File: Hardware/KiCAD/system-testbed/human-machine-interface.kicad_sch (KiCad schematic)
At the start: 2 parts, among them SW21 RotaryEncoder_Switch

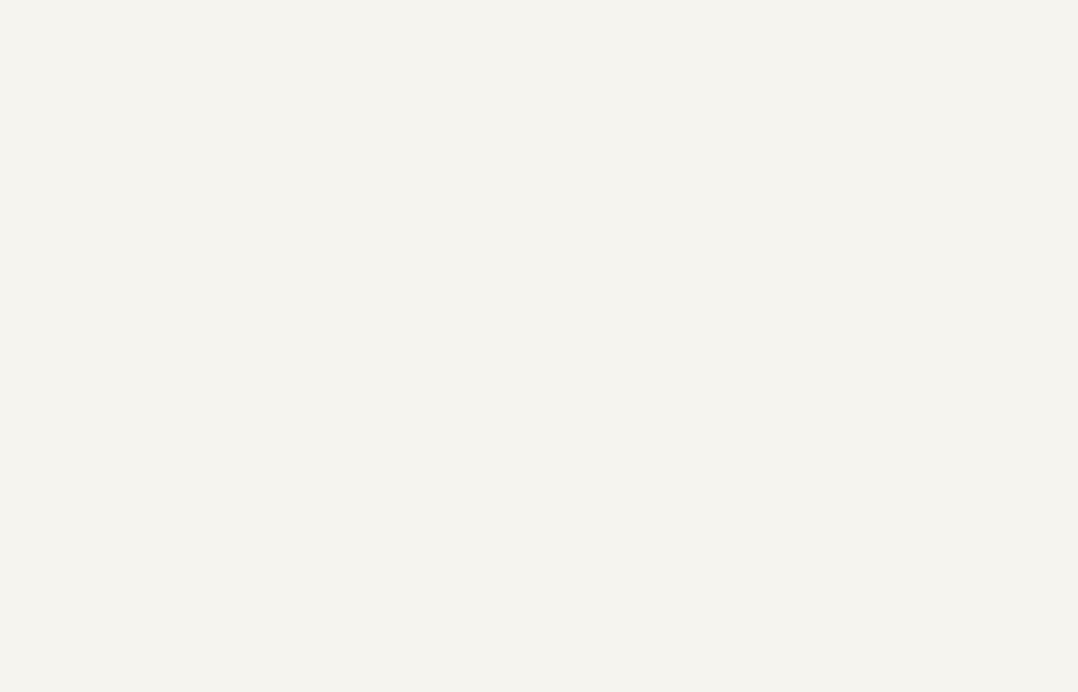
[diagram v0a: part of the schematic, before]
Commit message: feat: capture EYESPI display connectors #15
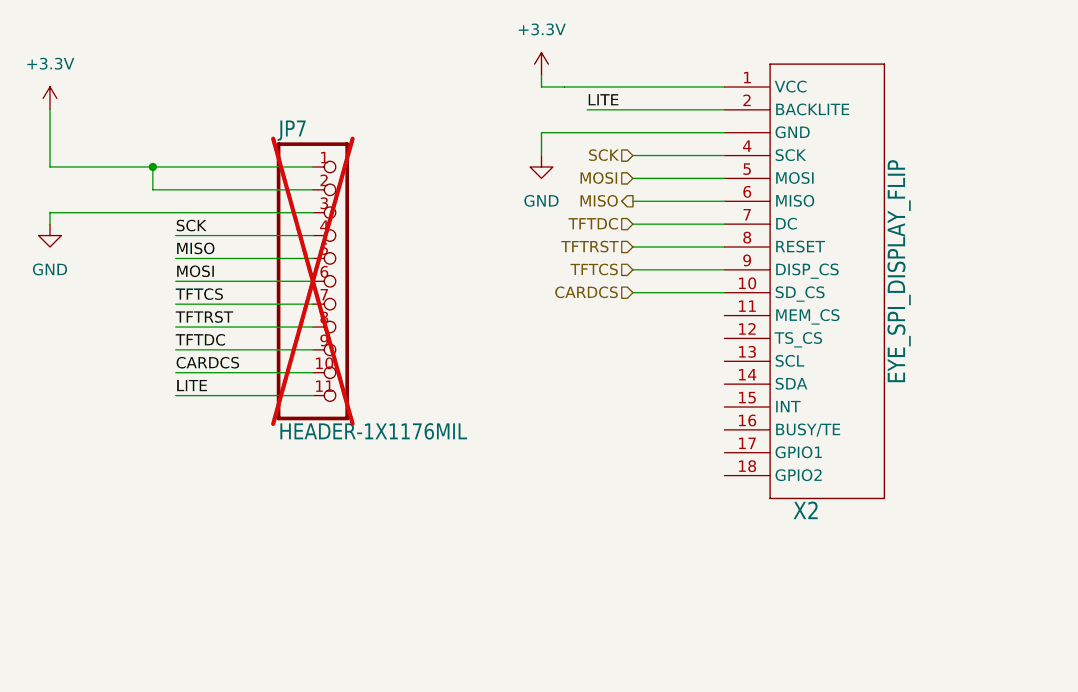
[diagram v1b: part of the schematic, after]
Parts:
- added JP7: HEADER-1X1176MIL, Display:1X11_ROUND_76, symbol Display-eagle-import:HEADER-1X1176MIL
- added X2: EYE_SPI_DISPLAY_FLIP, Display:EYE_SPI_DISPLAY_BOTCONTACT, symbol Display-eagle-import:EYE_SPI_DISPLAY_FLIP
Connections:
- net +3.3V: now also JP7.1, JP7.2, X2.1 (VCC)
- net GND: now also JP7.3, X2.3 (GND), X2.SUPPORT1 (GND), X2.SUPPORT2 (GND)
- new net CARDCS: JP7.10, X2.10 (SD_CS)
- new net LITE: JP7.11, X2.2 (BACKLITE)
- new net MISO: JP7.5, X2.6 (MISO)
- new net MOSI: JP7.6, X2.5 (MOSI)
- new net SCK: JP7.4, X2.4 (SCK)
- new net TFTCS: JP7.7, X2.9 (DISP_CS)
- new net TFTDC: JP7.9, X2.7 (DC)
- new net TFTRST: JP7.8, X2.8 (RESET)

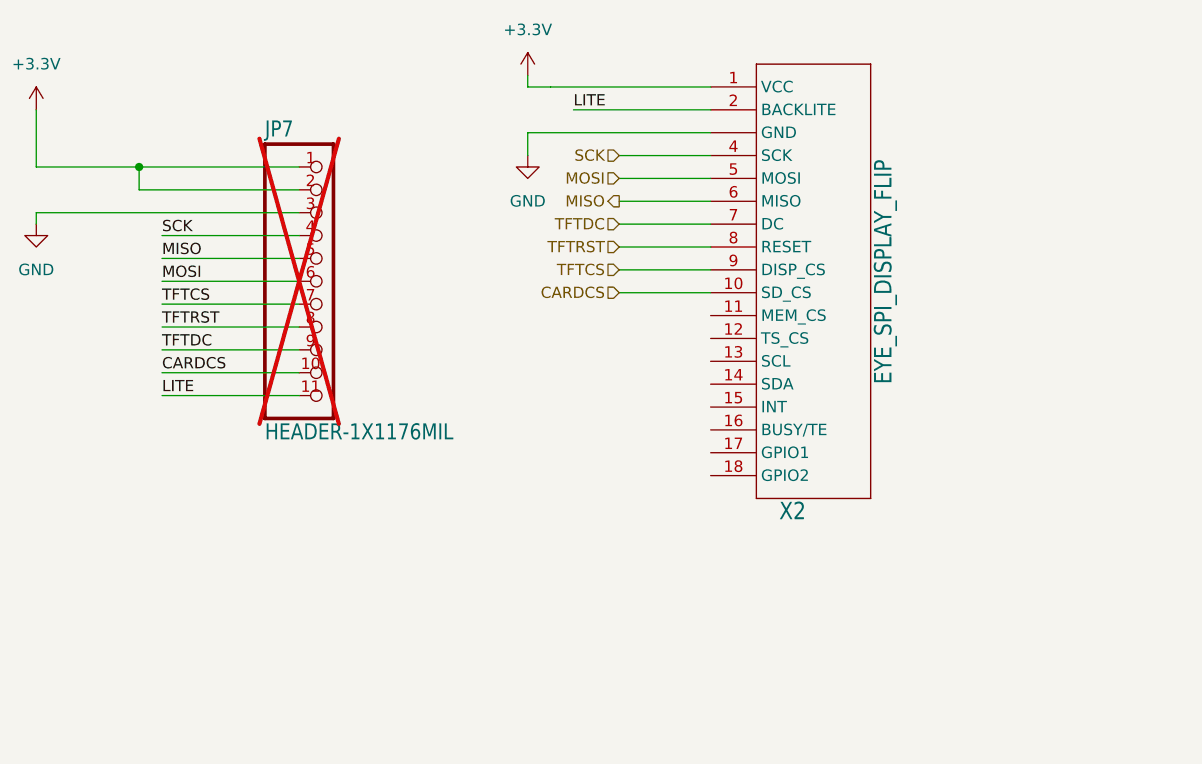
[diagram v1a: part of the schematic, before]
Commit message: fix: create real EYESPI FPC connector symbol and footprint #57
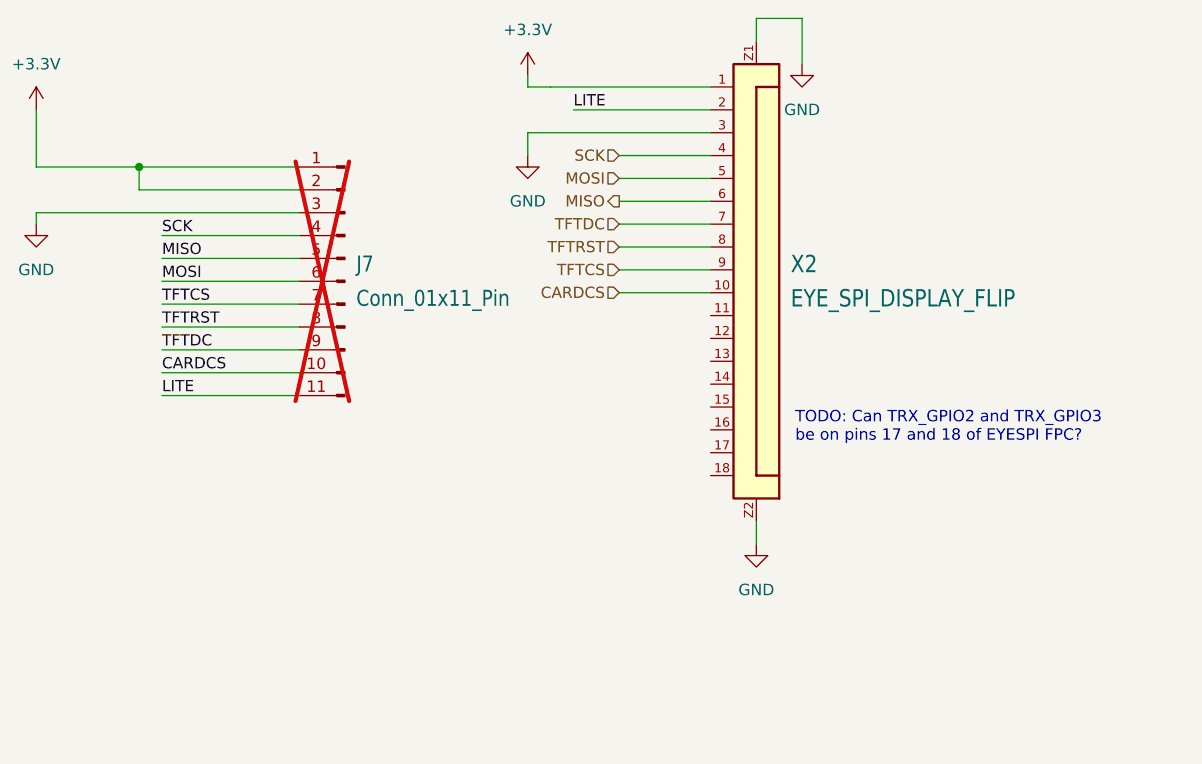
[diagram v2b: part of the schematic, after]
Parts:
- J7: renamed from JP7; value HEADER-1X1176MIL -> Conn_01x11_Pin; symbol Display-eagle-import:HEADER-1X1176MIL -> Connector:Conn_01x11_Pin
- X2: footprint Display:EYE_SPI_DISPLAY_BOTCONTACT -> capstone-project:Adafruit EYESPI FPC Connector; symbol Display-eagle-import:EYE_SPI_DISPLAY_FLIP -> capstone-project:Adafruit EYESPI FPC Connector
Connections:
- net GND: now also X2.Z1, X2.Z2; no longer X2.SUPPORT1 (GND), X2.SUPPORT2 (GND)
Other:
- note added: "TODO: Can TRX_GPIO2 and TRX_GPIO3 be on pins 17 and 18 of EYESPI FPC?"

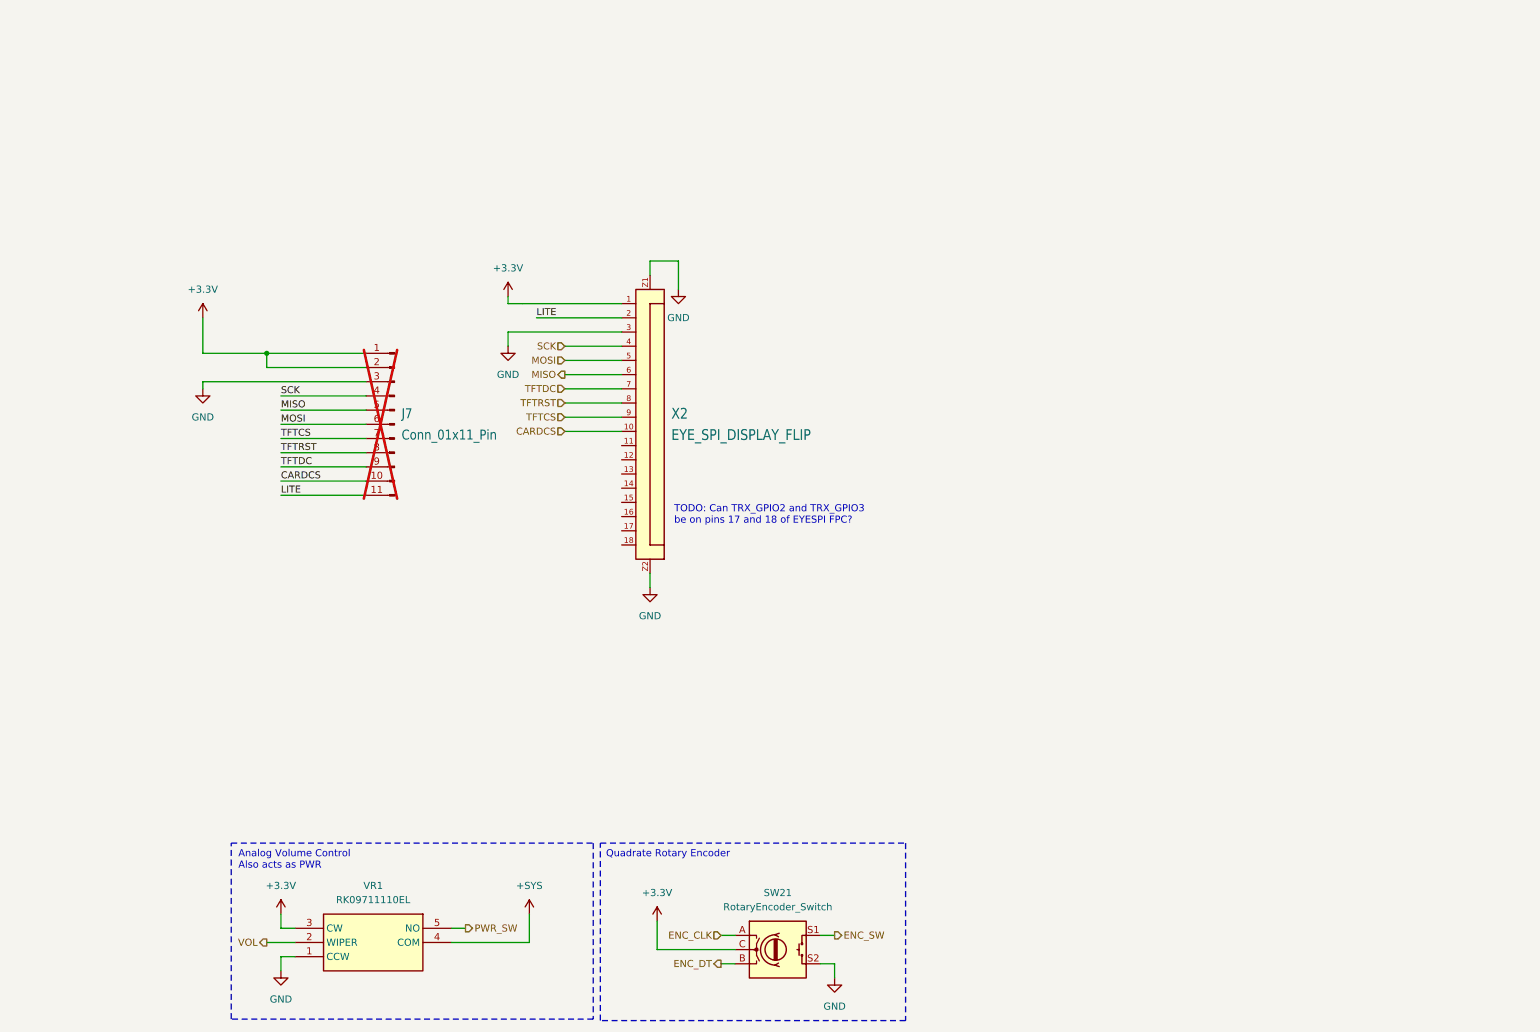
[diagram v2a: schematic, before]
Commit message: fix: move port expander over to HMI schematic #15 #33
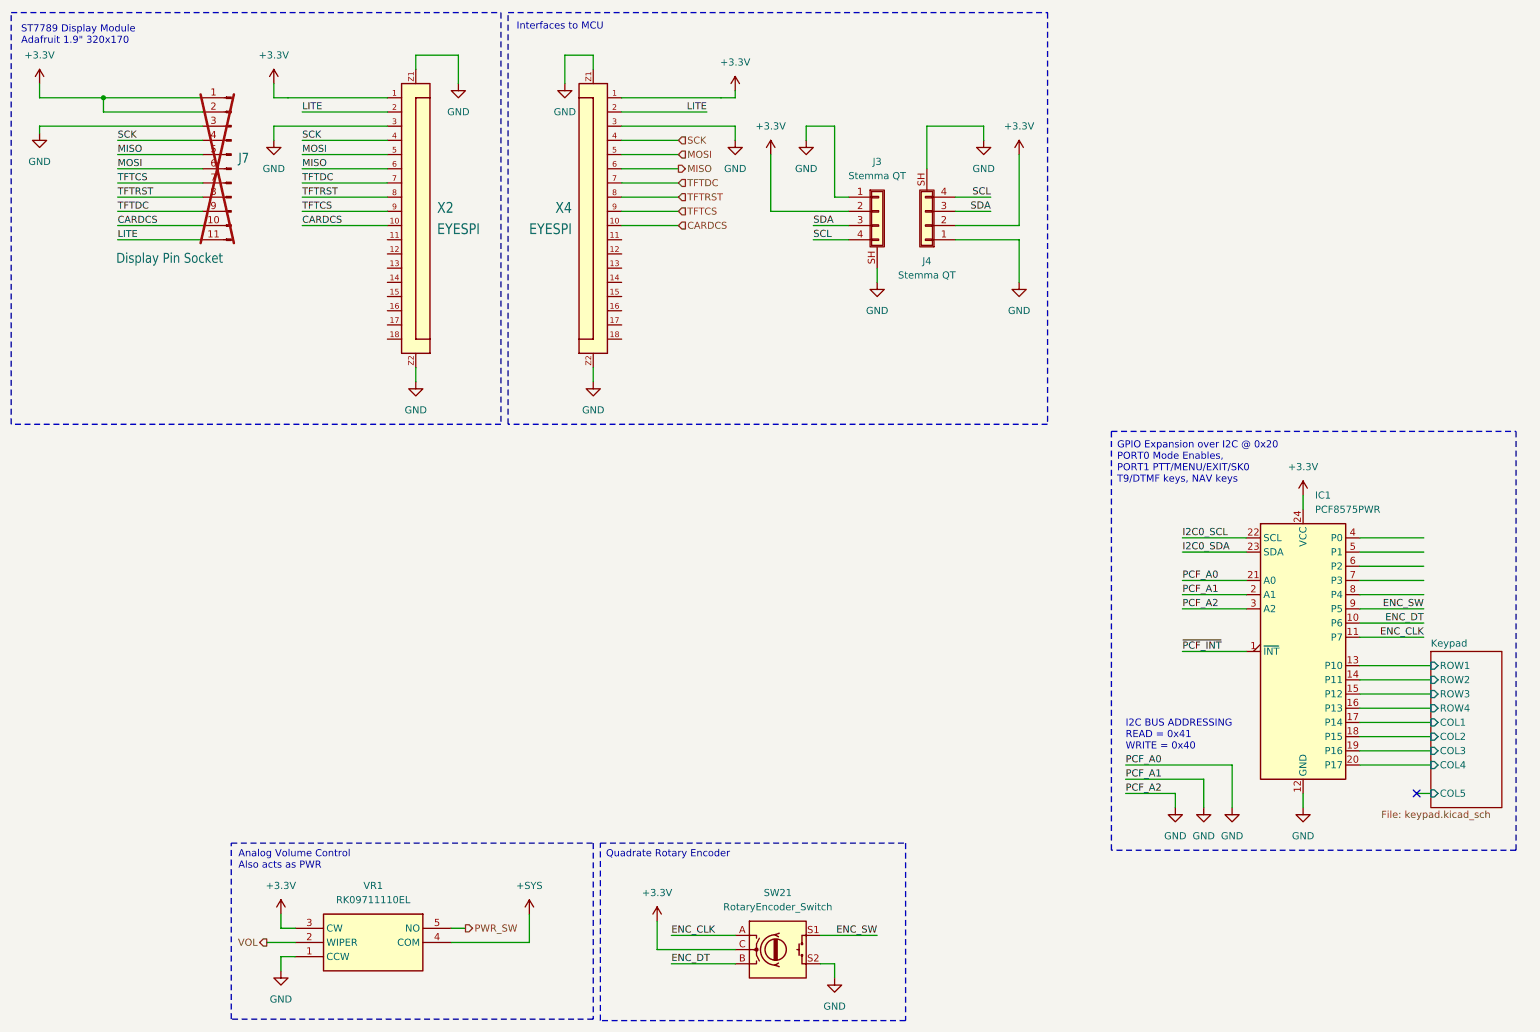
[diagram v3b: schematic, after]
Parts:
- added IC1: PCF8575PWR, Package_SO:SSOP-24_5.3x8.2mm_P0.65mm, symbol Interface_Expansion:PCF8575DBR
- added J3, J4: Stemma QT, Connector_JST:JST_SH_SM04B-SRSS-TB_1x04-1MP_P1.00mm_Horizontal, symbol Connector_Generic_Shielded:Conn_01x04_Shielded
- added X4: EYESPI, capstone-project:Adafruit EYESPI FPC Connector, symbol capstone-project:Adafruit EYESPI FPC Connector
- J7: value Conn_01x11_Pin -> Display Pin Socket
- X2: value EYE_SPI_DISPLAY_FLIP -> EYESPI
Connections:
- net +3.3V: now also IC1.24 (VCC), J3.2 (Pin_2), J4.2 (Pin_2), X4.1
- net CARDCS: now also X4.10
- net ENC_CLK: now also IC1.11 (P7)
- net ENC_DT: now also IC1.10 (P6)
- net ENC_SW: now also IC1.9 (P5)
- net GND: now also IC1.12 (GND), IC1.2 (A1), IC1.21 (A0), IC1.3 (A2), J3.1 (Pin_1), J3.SH (Shield), J4.1 (Pin_1), J4.SH (Shield), X4.3, X4.Z1, X4.Z2
- net LITE: now also X4.2
- net MISO: now also X4.6
- net MOSI: now also X4.5
- net SCK: now also X4.4
- net TFTCS: now also X4.9
- net TFTDC: now also X4.7
- net TFTRST: now also X4.8
- new net I2C0_SCL: IC1.22 (SCL)
- new net I2C0_SDA: IC1.23 (SDA)
- new net Keypad/COL1: IC1.17 (P14)
- new net Keypad/COL2: IC1.18 (P15)
- new net Keypad/COL3: IC1.19 (P16)
- new net Keypad/COL4: IC1.20 (P17)
- new net Keypad/ROW1: IC1.13 (P10)
- new net Keypad/ROW2: IC1.14 (P11)
- new net Keypad/ROW3: IC1.15 (P12)
- new net Keypad/ROW4: IC1.16 (P13)
- new net SCL: J3.4 (Pin_4), J4.4 (Pin_4)
- new net SDA: J3.3 (Pin_3), J4.3 (Pin_3)
- new net ~{PCF_INT}: IC1.1 (~{INT})
- no-connect marks 0 -> 1
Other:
- added sheet Keypad (keypad.kicad_sch)
- note added: "GPIO Expansion over I2C @ 0x20 PORT0 Mode Enables, PORT1 PTT/MENU/EXIT/SK0 T9/DTMF keys, NAV keys"
- note added: "I2C BUS ADDRESSING READ = 0x41 WRITE = 0x40"
- note added: "Interfaces to MCU"
- note added: "ST7789 Display Module Adafruit 1.9" 320x170"
- note removed: "TODO: Can TRX_GPIO2 and TRX_GPIO3 be on pins 17 and 18 of EYESPI FPC?"
- moved on the sheet: J7, X2

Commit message: Update-Jumper-Schematic
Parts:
- renumbered J7 to J1, J3 to J2, J4 to J3, SW21 to SW1, X2 to X1, X4 to X2

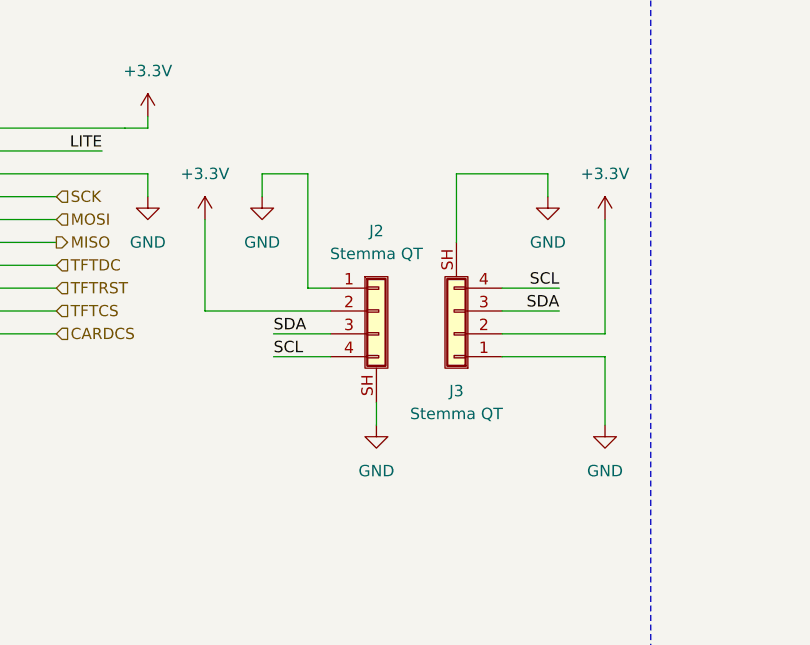
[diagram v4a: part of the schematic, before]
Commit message: fix: remove EYESPI from HMI sheet #69
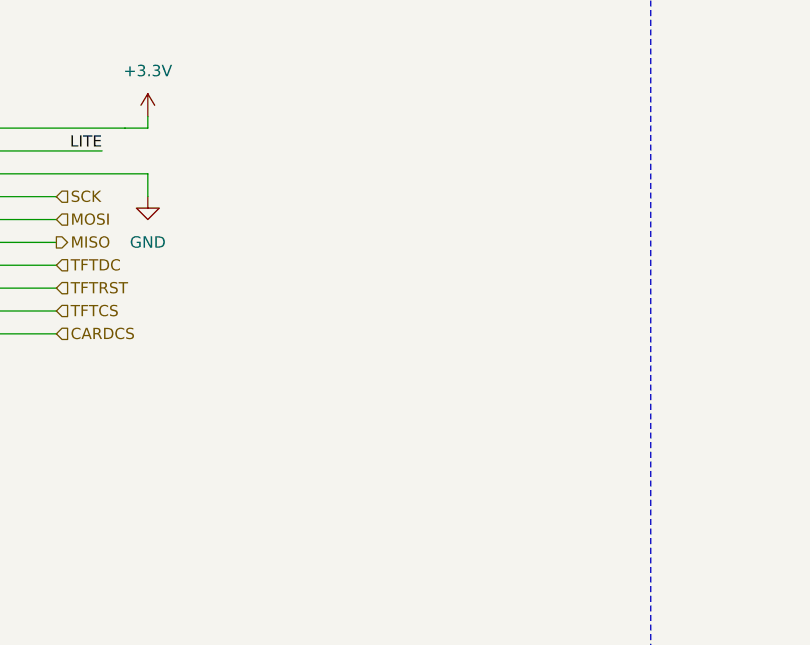
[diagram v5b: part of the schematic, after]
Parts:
- removed J2, J3: Stemma QT, Connector_JST:JST_SH_SM04B-SRSS-TB_1x04-1MP_P1.00mm_Horizontal, symbol Connector_Generic_Shielded:Conn_01x04_Shielded
